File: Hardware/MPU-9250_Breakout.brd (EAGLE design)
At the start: 17 x 17.8 mm, 18 parts, among them U1 MPU-9250

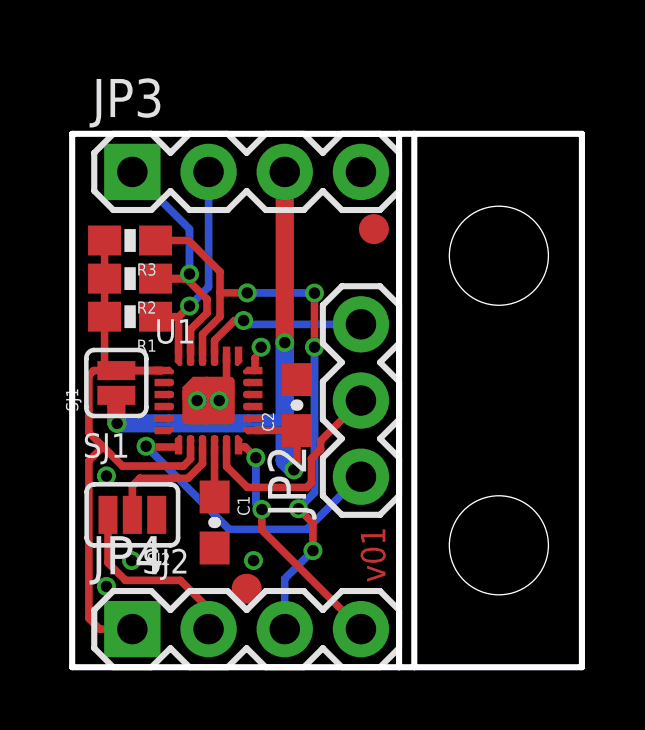
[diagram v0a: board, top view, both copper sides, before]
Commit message: Added axes
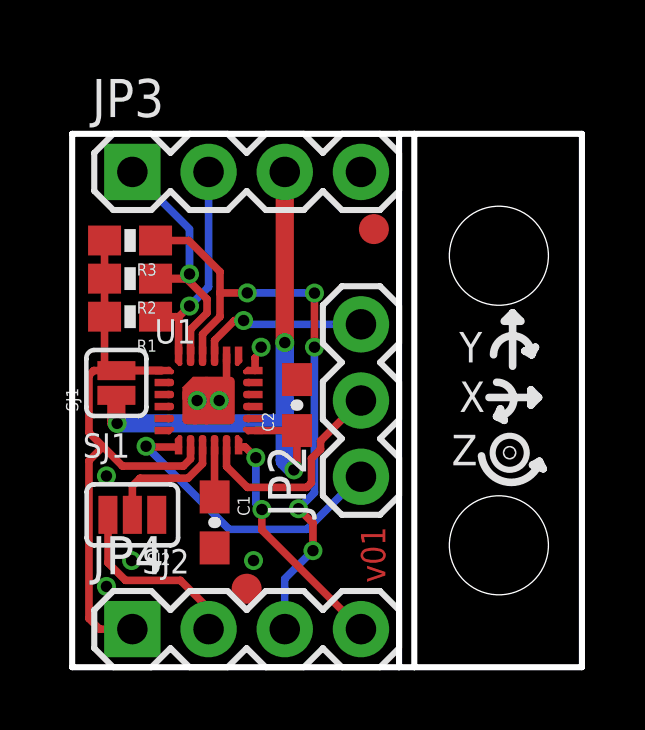
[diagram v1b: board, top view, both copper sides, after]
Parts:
- moved LOGO2 12.2 mm to (14.2, 8.51)
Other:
- board text added: "X"
- board text added: "Y"
- board text added: "Z"
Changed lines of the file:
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@@
 <layer number="45" name="Holes" color="7" fill="1" visible="yes" active="yes"/>
 <layer number="46" name="Milling" color="3" fill="1" visible="no" active="yes"/>
-<layer number="47" name="Measures" color="7" fill="1" visible="yes" active="yes"/>
+<layer number="47" name="Measures" color="7" fill="1" visible="no" active="yes"/>
 <layer number="48" name="Document" color="7" fill="1" visible="no" active="yes"/>
 <layer number="49" name="Reference" color="7" fill="1" visible="yes" active="yes"/>
@@
 <text x="2.3368" y="3.937" size="0.8128" layer="21" font="vector" ratio="15" align="top-left">SJ2</text>
 <text x="0.3556" y="7.7978" size="0.8128" layer="21" font="vector" ratio="15" align="top-left">SJ1</text>
+<wire x1="0.9652" y1="8.8646" x2="2.6162" y2="8.8646" width="0.254" layer="22"/>
+<wire x1="2.3622" y1="9.3726" x2="2.3622" y2="8.2296" width="0.254" layer="22" curve="180"/>
+<wire x1="2.3622" y1="8.2296" x2="2.1082" y2="8.1026" width="0.254" layer="22"/>
+<wire x1="2.3622" y1="8.2296" x2="2.2352" y2="8.4836" width="0.254" layer="22"/>
+<wire x1="0.9652" y1="8.8646" x2="1.2192" y2="9.1186" width="0.254" layer="22"/>
+<wire x1="0.9652" y1="8.8646" x2="1.2192" y2="8.6106" width="0.254" layer="22"/>
+<wire x1="1.8288" y1="11.684" x2="1.8288" y2="9.906" width="0.254" layer="22"/>
+<wire x1="2.4638" y1="10.287" x2="1.1938" y2="10.287" width="0.254" layer="22" curve="180"/>
+<wire x1="1.1938" y1="10.287" x2="1.0668" y2="10.541" width="0.254" layer="22"/>
+<wire x1="1.1938" y1="10.287" x2="1.4224" y2="10.414" width="0.254" layer="22"/>
+<wire x1="1.8288" y1="11.684" x2="2.0828" y2="11.43" width="0.254" layer="22"/>
+<wire x1="1.8288" y1="11.684" x2="1.5748" y2="11.43" width="0.254" layer="22"/>
+<wire x1="2.1082" y1="11.4046" x2="1.5494" y2="11.4046" width="0.254" layer="22"/>
+<wire x1="1.4224" y1="10.414" x2="1.0668" y2="10.541" width="0.254" layer="22"/>
+<wire x1="2.1082" y1="8.1026" x2="2.2352" y2="8.4836" width="0.254" layer="22"/>
+<wire x1="1.2192" y1="8.6106" x2="1.2192" y2="9.1186" width="0.254" layer="22"/>
+<text x="3.6068" y="10.033" size="1.016" layer="22" font="vector" ratio="20" rot="SMR0">Y</text>
+<text x="3.6068" y="8.382" size="1.016" layer="22" font="vector" ratio="20" rot="SMR0">X</text>
+<text x="3.8608" y="6.604" size="1.016" layer="22" font="vector" ratio="20" rot="SMR0">Z</text>
+<circle x="1.82371875" y="7.147559375" radius="0.5679" width="0.2032" layer="22"/>
+<wire x1="2.77368125" y1="6.817359375" x2="2.90068125" y2="6.563359375" width="0.254" layer="22"/>
+<wire x1="2.77368125" y1="6.817359375" x2="2.54508125" y2="6.690359375" width="0.254" layer="22"/>
+<wire x1="2.54508125" y1="6.690359375" x2="2.90068125" y2="6.563359375" width="0.254" layer="22"/>
+<wire x1="2.77368125" y1="6.766559375" x2="0.84328125" y2="6.995159375" width="0.254" layer="22" curve="-153.372806"/>
+<wire x1="15.5448" y1="8.9916" x2="13.8938" y2="8.9916" width="0.254" layer="21"/>
+<wire x1="14.1478" y1="9.4996" x2="14.1478" y2="8.3566" width="0.254" layer="21" curve="-180"/>
+<wire x1="14.1478" y1="8.3566" x2="14.4018" y2="8.2296" width="0.254" layer="21"/>
+<wire x1="14.1478" y1="8.3566" x2="14.2748" y2="8.6106" width="0.254" layer="21"/>
+<wire x1="15.5448" y1="8.9916" x2="15.2908" y2="9.2456" width="0.254" layer="21"/>
+<wire x1="15.5448" y1="8.9916" x2="15.2908" y2="8.7376" width="0.254" layer="21"/>
+<wire x1="14.6812" y1="11.811" x2="14.6812" y2="10.033" width="0.254" layer="21"/>
+<wire x1="14.0462" y1="10.414" x2="15.3162" y2="10.414" width="0.254" layer="21" curve="-180"/>
+<wire x1="15.3162" y1="10.414" x2="15.4432" y2="10.668" width="0.254" layer="21"/>
+<wire x1="15.3162" y1="10.414" x2="15.0876" y2="10.541" width="0.254" layer="21"/>
+<wire x1="14.6812" y1="11.811" x2="14.4272" y2="11.557" width="0.254" layer="21"/>
+<wire x1="14.6812" y1="11.811" x2="14.9352" y2="11.557" width="0.254" layer="21"/>
+<wire x1="14.4018" y1="11.5316" x2="14.9606" y2="11.5316" width="0.254" layer="21"/>
+<wire x1="15.0876" y1="10.541" x2="15.4432" y2="10.668" width="0.254" layer="21"/>
+<wire x1="14.4018" y1="8.2296" x2="14.2748" y2="8.6106" width="0.254" layer="21"/>
+<wire x1="15.2908" y1="8.7376" x2="15.2908" y2="9.2456" width="0.254" layer="21"/>
+<text x="12.9032" y="10.16" size="1.016" layer="21" font="vector" ratio="20" rot="SR0">Y</text>
+<text x="12.9032" y="8.509" size="1.016" layer="21" font="vector" ratio="20" rot="SR0">X</text>
+<text x="12.6492" y="6.731" size="1.016" layer="21" font="vector" ratio="20" rot="SR0">Z</text>
+<circle x="14.58468125" y="7.147559375" radius="0.5679" width="0.2032" layer="21"/>
+<wire x1="15.57528125" y1="6.868159375" x2="15.70228125" y2="6.614159375" width="0.254" layer="21"/>
+<wire x1="15.57528125" y1="6.868159375" x2="15.34668125" y2="6.741159375" width="0.254" layer="21"/>
+<wire x1="15.34668125" y1="6.741159375" x2="15.70228125" y2="6.614159375" width="0.254" layer="21"/>
+<wire x1="15.57528125" y1="6.817359375" x2="13.64488125" y2="7.045959375" width="0.254" layer="21" curve="-153.372806"/>
+<circle x="14.582140625" y="7.1501" radius="0.0254" width="0.4064" layer="21"/>
+<wire x1="1.4732" y1="7.5692" x2="2.2098" y2="6.8326" width="0.254" layer="22"/>
+<wire x1="2.1844" y1="7.5692" x2="1.4478" y2="6.8326" width="0.254" layer="22"/>
 </plain>
 <attributes>
@@
 </element>
 <element name="LOGO1" library="SparkFun-Aesthetics" package="SFE_LOGO_FLAME_.1" value="SFE_LOGO_FLAME.1_INCH" x="4.6228" y="10.3632" rot="MR0"/>
-<element name="LOGO2" library="SparkFun-Aesthetics" package="OSHW-LOGO-S" value="OSHW-LOGOS" x="2.0574" y="7.4422" rot="MR0"/>
+<element name="LOGO2" library="SparkFun-Aesthetics" package="OSHW-LOGO-S" value="OSHW-LOGOS" x="14.224" y="8.509" rot="MR0"/>
 <element name="STANDOFF1" library="SparkFun-Electromechanical" package="STAND-OFF" value="STAND-OFF" x="14.224" y="4.064"/>
 <element name="STANDOFF2" library="SparkFun-Electromechanical" package="STAND-OFF" value="STAND-OFF" x="14.224" y="13.716"/>
